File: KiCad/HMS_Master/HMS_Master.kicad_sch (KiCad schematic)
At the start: 1 part, among them U1 ESP32-DEVKITC-32UE

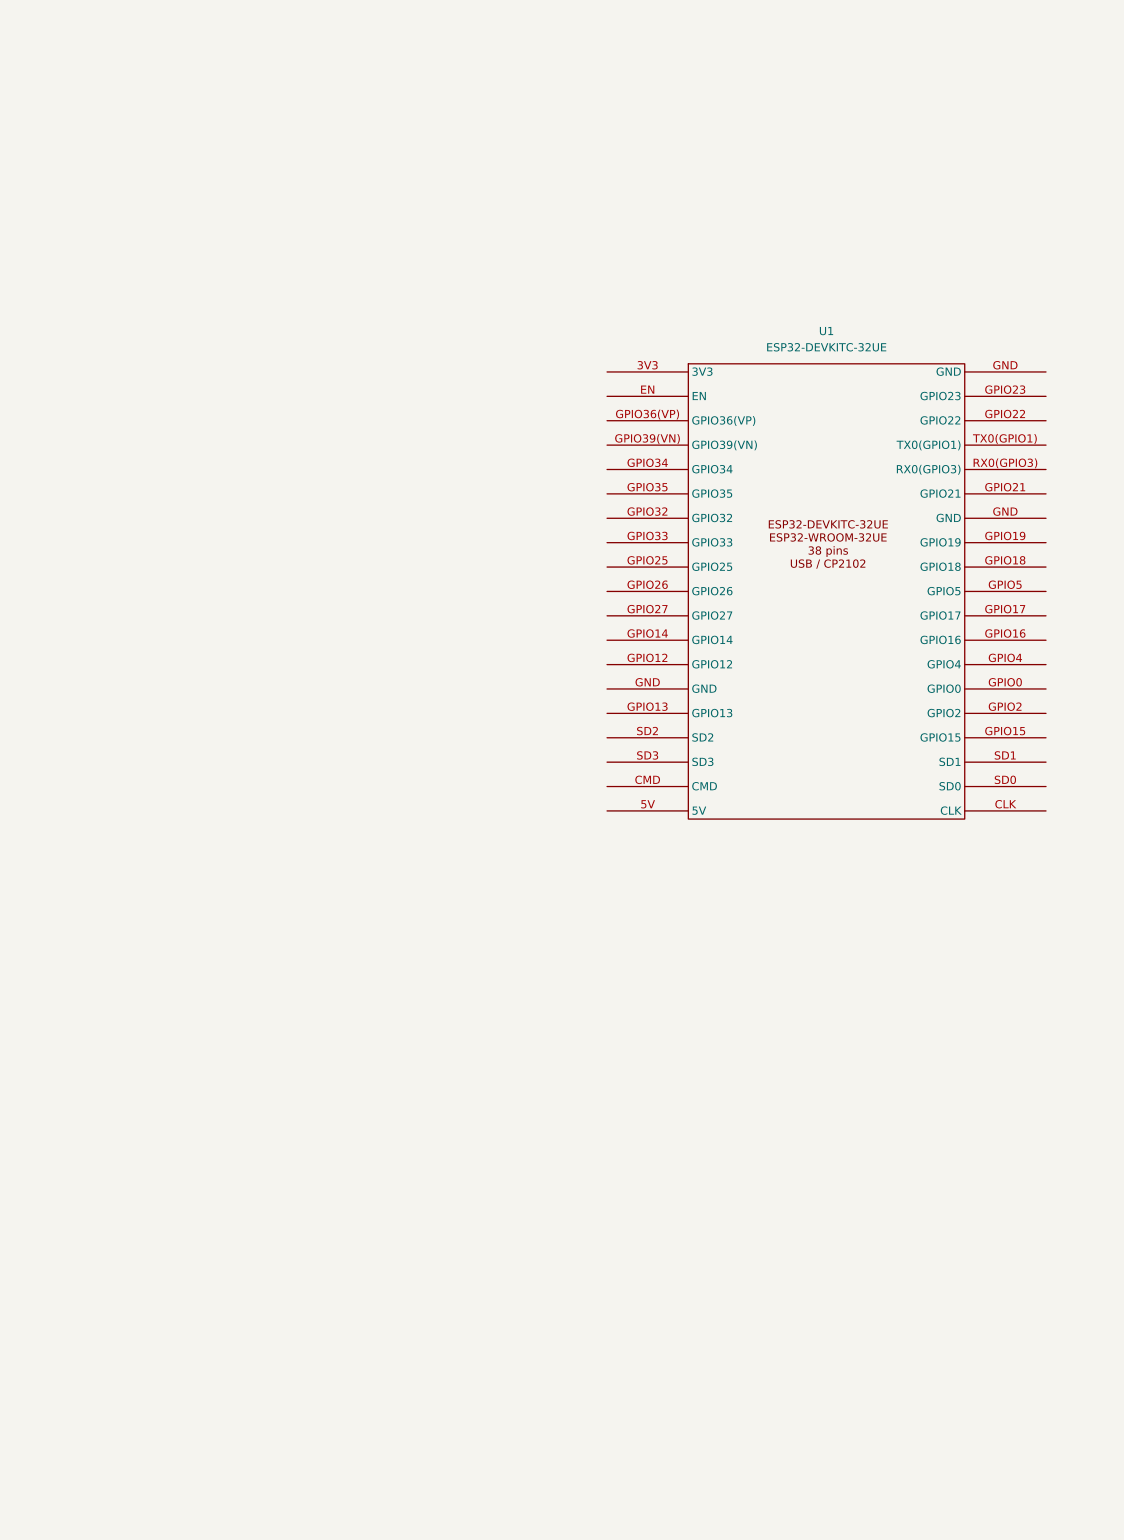
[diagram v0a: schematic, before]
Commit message: Create power supply block and clean ERC
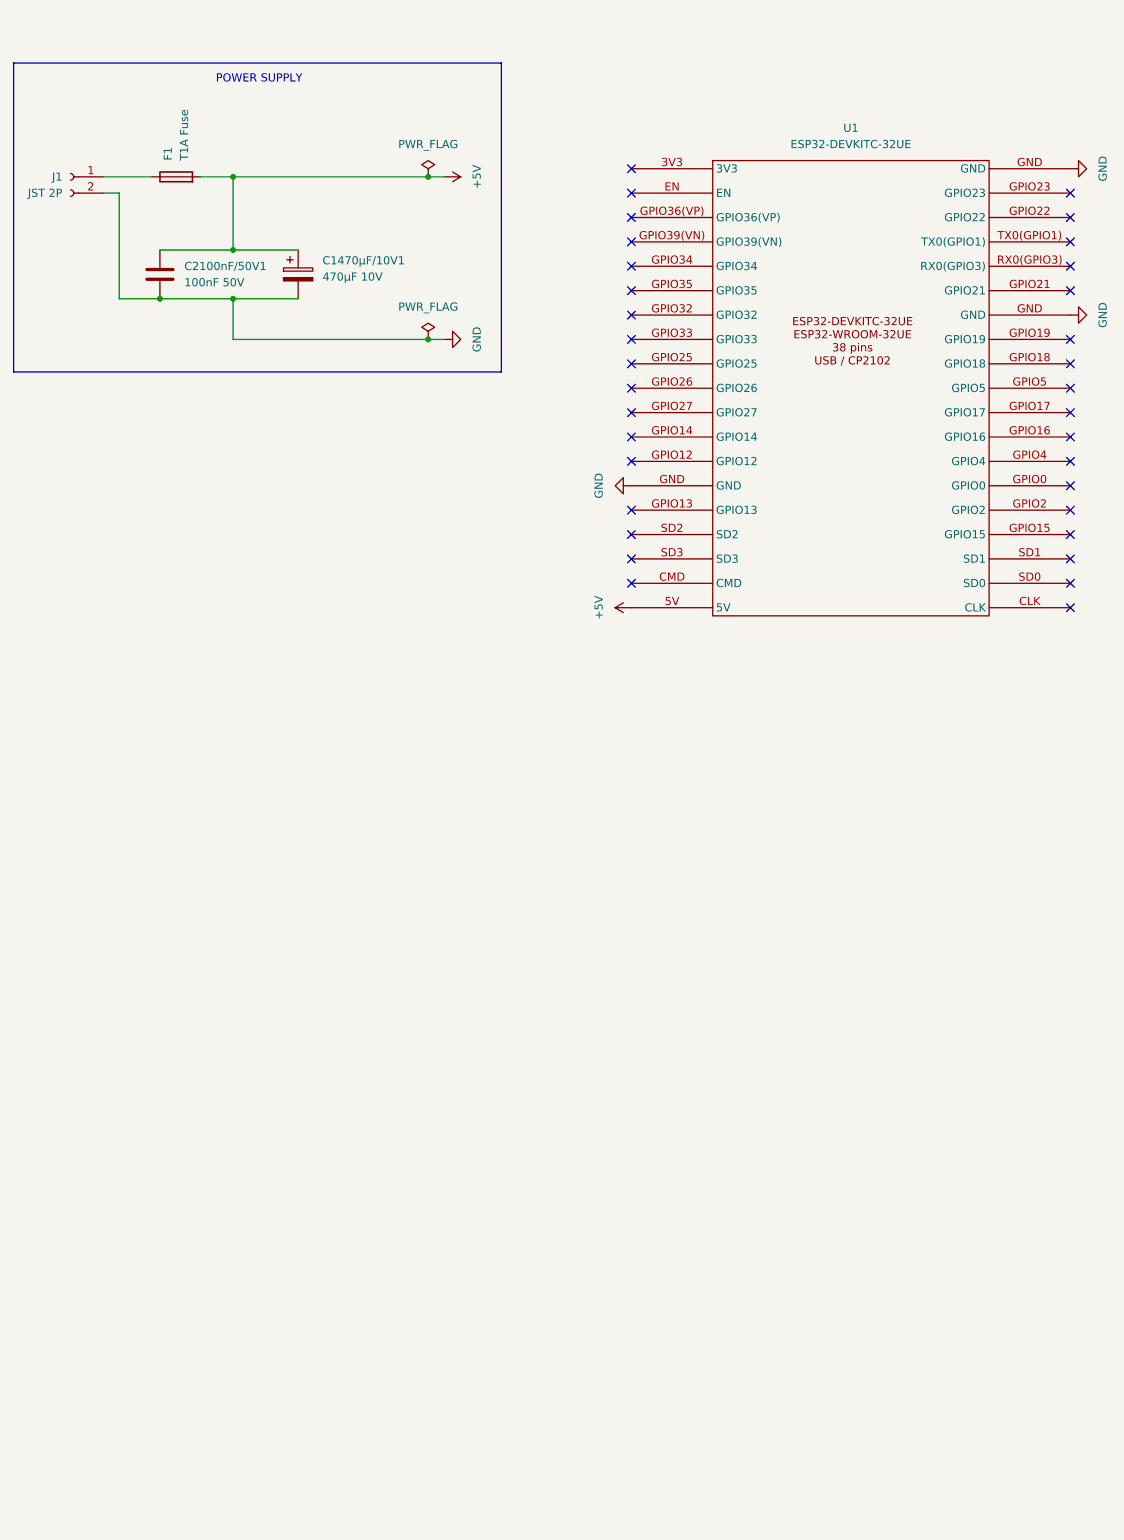
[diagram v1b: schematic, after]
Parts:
- added C1470µF/10V1: 470µF 10V, symbol Device:C_Polarized
- added C2100nF/50V1: 100nF 50V, symbol Device:C
- added F1: T1A Fuse, symbol Device:Fuse
- added J1: JST 2P, symbol Connector:Conn_01x02_Socket
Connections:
- net +5V: now reaches U1.5V
- net +5V: now also C1470µF/10V1.1, C2100nF/50V1.1, F1.2
- net GND: now reaches U1.GND
- net GND: now also C1470µF/10V1.2, C2100nF/50V1.2, J1.2 (Pin_2)
- new net: F1.1, J1.1 (Pin_1)
- no-connect marks 0 -> 34
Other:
- note added: "POWER SUPPLY"
- moved on the sheet: U1

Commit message: Schematic Complete
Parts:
- removed C1470µF/10V1: 470µF 10V, symbol Device:C_Polarized
- removed C2100nF/50V1: 100nF 50V, symbol Device:C
- removed F1: T1A Fuse, symbol Device:Fuse
- removed J1: JST 2P, symbol Connector:Conn_01x02_Socket
- removed U1: ESP32-DEVKITC-32UE, symbol HMS_Symbols:ESP32_DEVKITC_32UE
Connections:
- no-connect marks 34 -> 0
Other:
- added sheet 01_ESP32 (../Sheets/01_ESP32.kicad_sch)
- added sheet 02_Power_Supply (../Sheets/02_Power_Supply.kicad_sch)
- added sheet 03_Display (../Sheets/03_Display.kicad_sch)
- added sheet 04_Chimney_Temperature (..\Sheets\04_Chimney_Temperature.kicad_sch)
- added sheet 05_Temperature_Sensors (..\Sheets\05_Temperature_Sensors.kicad_sch)
- added sheet 06_RTC (..\Sheets\06_RTC.kicad_sch)
- added sheet 07_Buzzer (..\Sheets\07_Buzzer.kicad_sch)
- added sheet 08_Boiler_Room_Sensor (..\Sheets\08_Boiler_Room_Sensor.kicad_sch)
- added sheet 09_MicroSD (..\Sheets\09_MicroSD.kicad_sch)
- added sheet 10_Voltage_Detectors (..\Sheets\10_Voltage_Detectors.kicad_sch)
- note removed: "POWER SUPPLY"

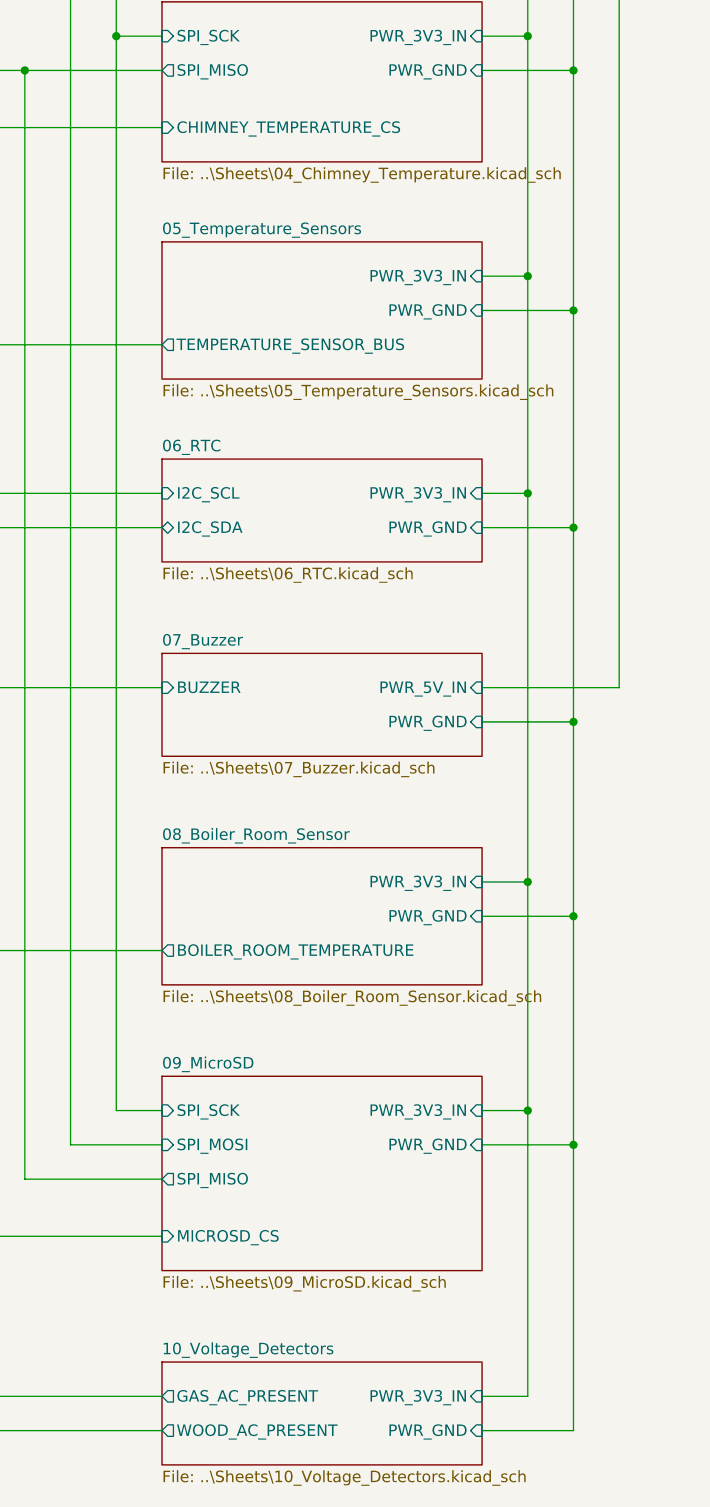
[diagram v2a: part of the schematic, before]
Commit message: Footprints are created and assigned
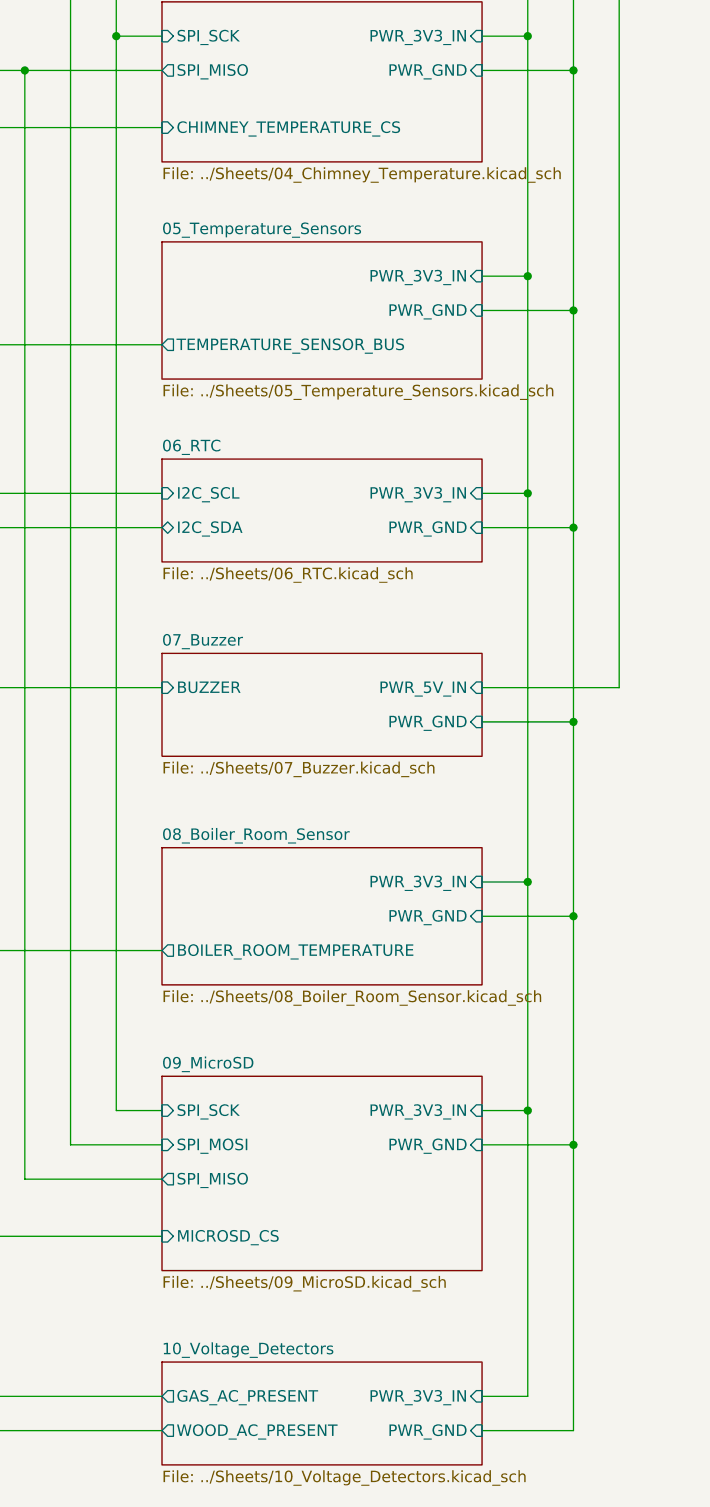
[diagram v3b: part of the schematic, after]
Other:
- sheet 04_Chimney_Temperature: file ..\Sheets\04_Chimney_Temperature.kicad_sch -> ../Sheets/04_Chimney_Temperature.kicad_sch
- sheet 05_Temperature_Sensors: file ..\Sheets\05_Temperature_Sensors.kicad_sch -> ../Sheets/05_Temperature_Sensors.kicad_sch
- sheet 06_RTC: file ..\Sheets\06_RTC.kicad_sch -> ../Sheets/06_RTC.kicad_sch
- sheet 07_Buzzer: file ..\Sheets\07_Buzzer.kicad_sch -> ../Sheets/07_Buzzer.kicad_sch
- sheet 08_Boiler_Room_Sensor: file ..\Sheets\08_Boiler_Room_Sensor.kicad_sch -> ../Sheets/08_Boiler_Room_Sensor.kicad_sch
- sheet 09_MicroSD: file ..\Sheets\09_MicroSD.kicad_sch -> ../Sheets/09_MicroSD.kicad_sch
- sheet 10_Voltage_Detectors: file ..\Sheets\10_Voltage_Detectors.kicad_sch -> ../Sheets/10_Voltage_Detectors.kicad_sch
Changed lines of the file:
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@@
 			)
 		)
-		(property "Sheetfile" "..\\Sheets\\08_Boiler_Room_Sensor.kicad_sch"
+		(property "Sheetfile" "../Sheets/08_Boiler_Room_Sensor.kicad_sch"
 			(at 101.6 194.8946 0)
 			(show_name no)
@@
 			)
 		)
-		(property "Sheetfile" "..\\Sheets\\06_RTC.kicad_sch"
+		(property "Sheetfile" "../Sheets/06_RTC.kicad_sch"
 			(at 101.6 147.9046 0)
 			(show_name no)
@@
 			)
 		)
-		(property "Sheetfile" "..\\Sheets\\07_Buzzer.kicad_sch"
+		(property "Sheetfile" "../Sheets/07_Buzzer.kicad_sch"
 			(at 101.6 169.4946 0)
 			(show_name no)
@@
 			)
 		)
-		(property "Sheetfile" "..\\Sheets\\09_MicroSD.kicad_sch"
+		(property "Sheetfile" "../Sheets/09_MicroSD.kicad_sch"
 			(at 101.6 226.6446 0)
 			(show_name no)
@@
 			)
 		)
-		(property "Sheetfile" "..\\Sheets\\10_Voltage_Detectors.kicad_sch"
+		(property "Sheetfile" "../Sheets/10_Voltage_Detectors.kicad_sch"
 			(at 101.6 248.2346 0)
 			(show_name no)
@@
 			)
 		)
-		(property "Sheetfile" "..\\Sheets\\05_Temperature_Sensors.kicad_sch"
+		(property "Sheetfile" "../Sheets/05_Temperature_Sensors.kicad_sch"
 			(at 101.6 127.5846 0)
 			(show_name no)
@@
 			)
 		)
-		(property "Sheetfile" "..\\Sheets\\04_Chimney_Temperature.kicad_sch"
+		(property "Sheetfile" "../Sheets/04_Chimney_Temperature.kicad_sch"
 			(at 101.6 103.4546 0)
 			(show_name no)

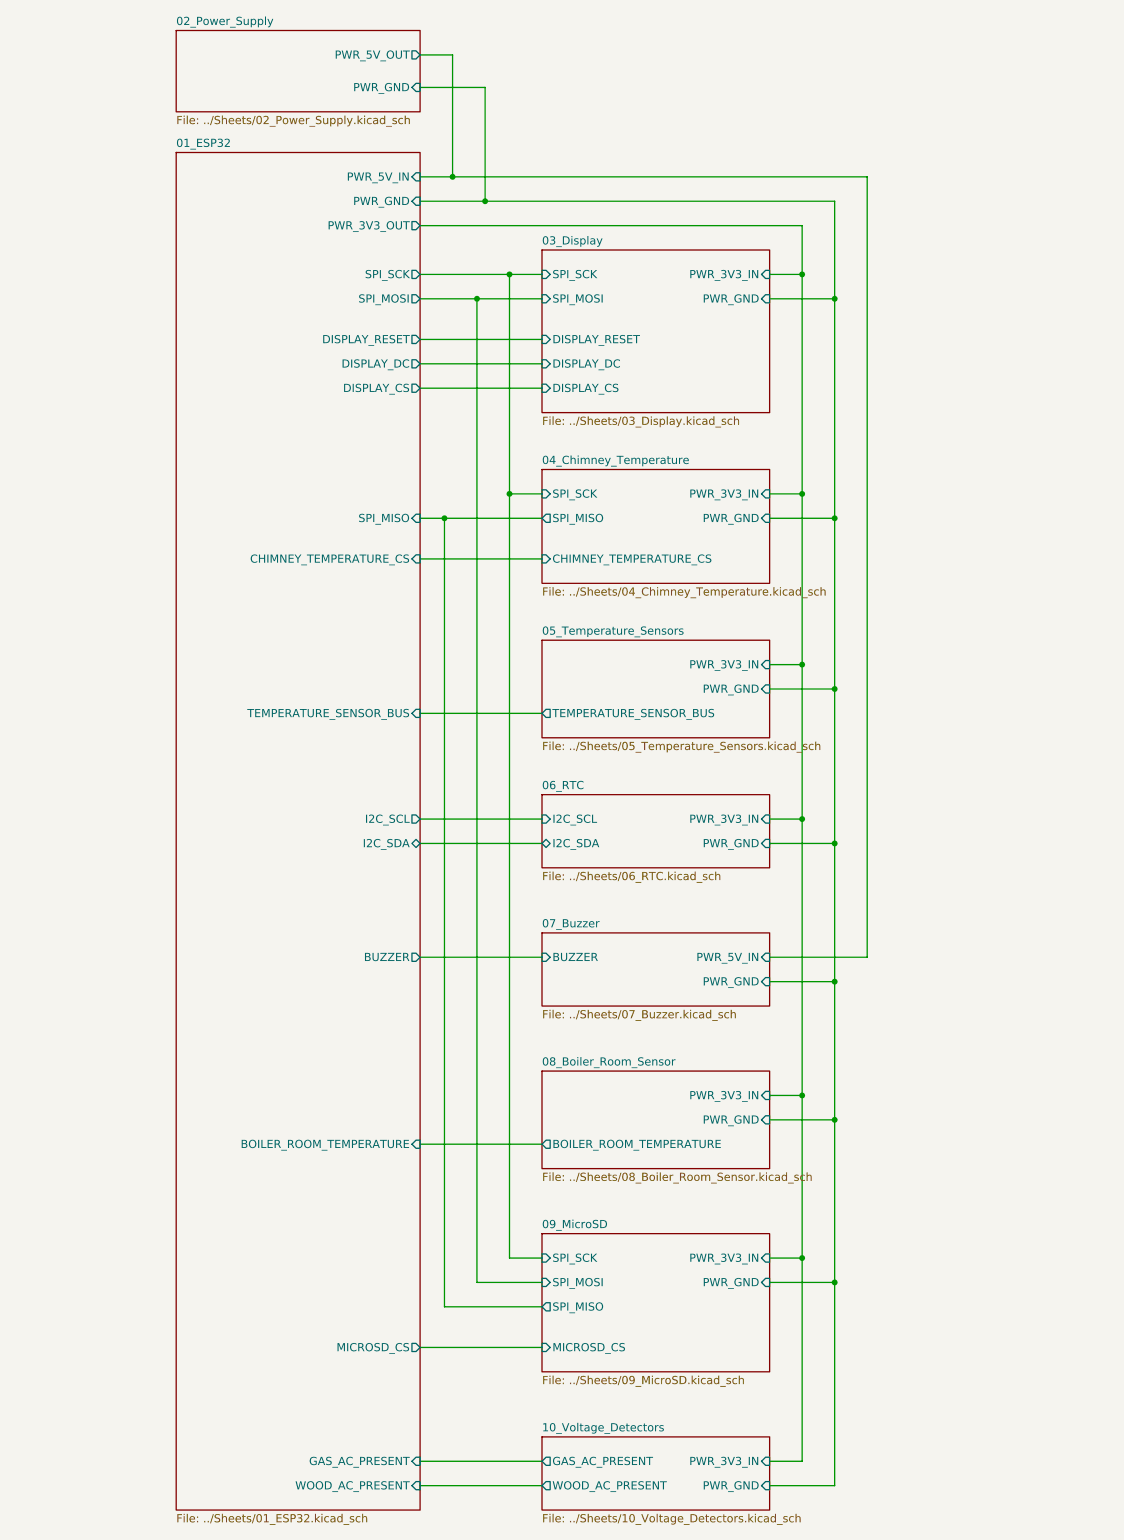
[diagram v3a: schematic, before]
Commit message: LEDs sheet added, schematic finished
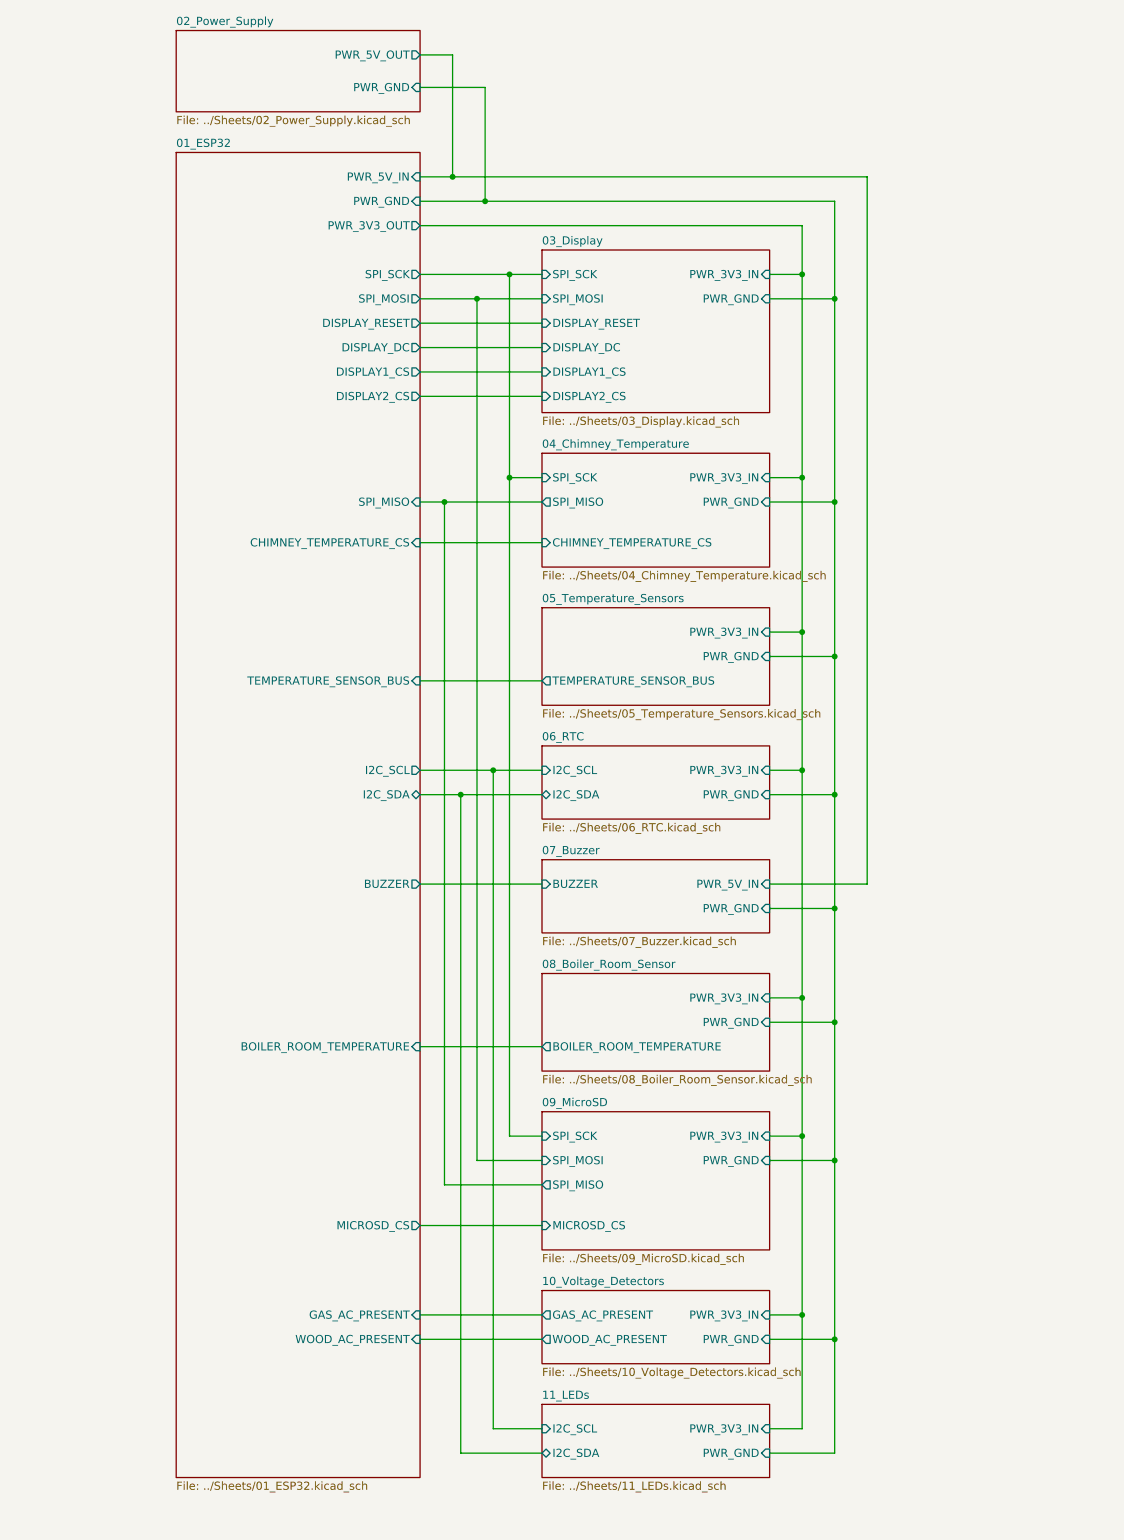
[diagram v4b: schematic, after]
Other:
- added sheet 11_LEDs (../Sheets/11_LEDs.kicad_sch)
- sheet 01_ESP32 ports: added DISPLAY1_CS, DISPLAY2_CS; removed DISPLAY_CS
- sheet 03_Display ports: added DISPLAY1_CS, DISPLAY2_CS; removed DISPLAY_CS
